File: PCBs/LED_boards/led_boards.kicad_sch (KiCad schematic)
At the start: 14 parts, among them J1 from_shield, J2 from_shield

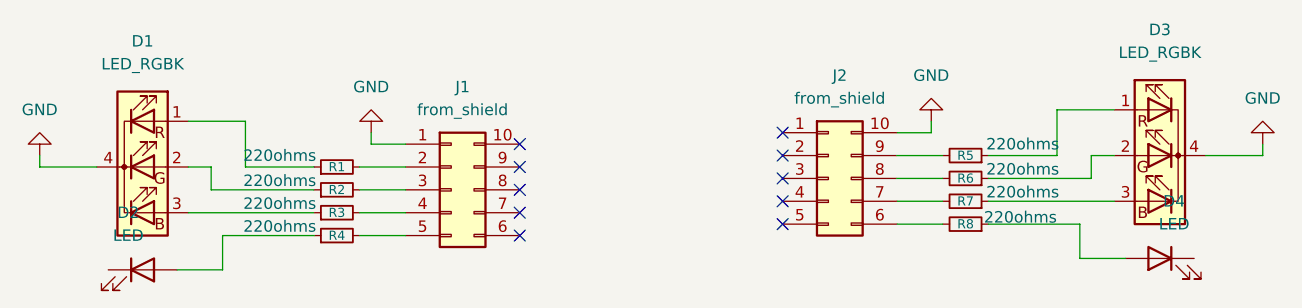
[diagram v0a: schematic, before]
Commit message: create parts for 3D printing
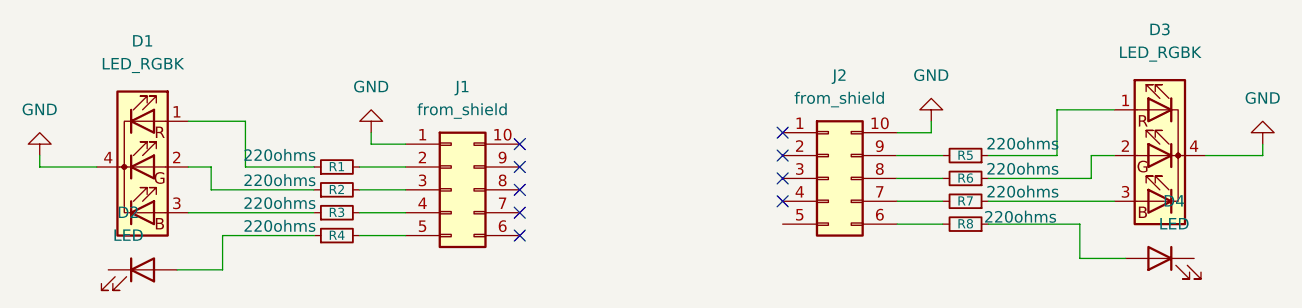
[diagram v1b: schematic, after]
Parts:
- D1, D3: footprint LED_THT:LED_D5.0mm-4_RGB_Wide_Pins -> (none)
- D2, D4: footprint LED_THT:LED_D5.0mm -> (none)
- J1, J2: footprint Connector_IDC:IDC-Header_2x05_P2.54mm_Vertical -> (none)
- R1, R2, R3, R4, R5, R6, R7, R8: footprint Resistor_THT:R_Axial_DIN0309_L9.0mm_D3.2mm_P12.70mm_Horizontal -> (none)
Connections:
- no-connect marks 10 -> 9
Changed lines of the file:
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@@
-	)
-	(no_connect
-		(at 153.67 71.12)
 	)
 	(no_connect
@@
 			)
 		)
-		(property "Footprint" "Resistor_THT:R_Axial_DIN0309_L9.0mm_D3.2mm_P12.70mm_Horizontal"
+		(property "Footprint" ""
 			(at 173.99 63.5 0)
 			(effects
@@
 			)
 		)
-		(property "Footprint" "LED_THT:LED_D5.0mm-4_RGB_Wide_Pins"
+		(property "Footprint" ""
 			(at 195.58 64.77 0)
 			(effects
@@
 			)
 		)
-		(property "Footprint" "Resistor_THT:R_Axial_DIN0309_L9.0mm_D3.2mm_P12.70mm_Horizontal"
+		(property "Footprint" ""
 			(at 104.14 67.31 0)
 			(effects
@@
 			)
 		)
-		(property "Footprint" "Resistor_THT:R_Axial_DIN0309_L9.0mm_D3.2mm_P12.70mm_Horizontal"
+		(property "Footprint" ""
 			(at 173.99 66.04 0)
 			(effects
@@
 			)
 		)
-		(property "Footprint" "Connector_IDC:IDC-Header_2x05_P2.54mm_Vertical"
+		(property "Footprint" ""
 			(at 116.84 67.31 0)
 			(effects
@@
 			)
 		)
-		(property "Footprint" "Resistor_THT:R_Axial_DIN0309_L9.0mm_D3.2mm_P12.70mm_Horizontal"
+		(property "Footprint" ""
 			(at 173.99 68.58 0)
 			(effects
@@
 			)
 		)
-		(property "Footprint" "Connector_IDC:IDC-Header_2x05_P2.54mm_Vertical"
+		(property "Footprint" ""
 			(at 158.75 66.04 0)
 			(effects
@@
 			)
 		)
-		(property "Footprint" "Resistor_THT:R_Axial_DIN0309_L9.0mm_D3.2mm_P12.70mm_Horizontal"
+		(property "Footprint" ""
 			(at 104.14 72.39 0)
 			(effects
@@
 			)
 		)
-		(property "Footprint" "LED_THT:LED_D5.0mm-4_RGB_Wide_Pins"
+		(property "Footprint" ""
 			(at 82.55 66.04 0)
 			(effects
@@
 			)
 		)
-		(property "Footprint" "Resistor_THT:R_Axial_DIN0309_L9.0mm_D3.2mm_P12.70mm_Horizontal"
+		(property "Footprint" ""
 			(at 104.14 69.85 0)
 			(effects
@@
 			)
 		)
-		(property "Footprint" "Resistor_THT:R_Axial_DIN0309_L9.0mm_D3.2mm_P12.70mm_Horizontal"
+		(property "Footprint" ""
 			(at 173.99 71.12 0)
 			(effects
@@
 			)
 		)
-		(property "Footprint" "Resistor_THT:R_Axial_DIN0309_L9.0mm_D3.2mm_P12.70mm_Horizontal"
+		(property "Footprint" ""
 			(at 104.14 64.77 0)
 			(effects
@@
 			)
 		)
-		(property "Footprint" "LED_THT:LED_D5.0mm"
+		(property "Footprint" ""
 			(at 82.55 76.2 0)
 			(effects
@@
 			)
 		)
-		(property "Footprint" "LED_THT:LED_D5.0mm"
+		(property "Footprint" ""
 			(at 195.58 74.93 0)
 			(effects

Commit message: update bom and finish first version of PCBs
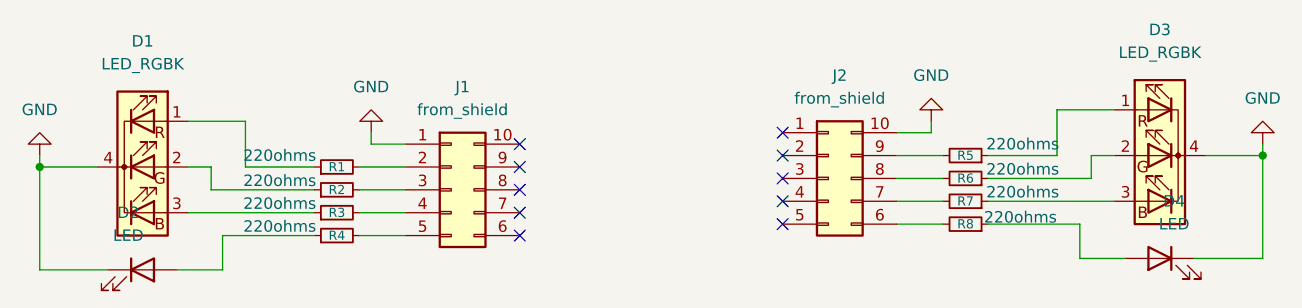
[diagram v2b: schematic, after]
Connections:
- net GND: now also D2.1 (K), D4.1 (K)
- no-connect marks 9 -> 10
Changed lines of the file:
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@@
 	(generator_version "9.0")
 	(paper "A4")
+	(junction
+		(at 207.01 63.5)
+		(diameter 0)
+		(color 0 0 0 0)
+	)
+	(junction
+		(at 71.12 64.77)
+		(diameter 0)
+		(color 0 0 0 0)
+	)
 	(no_connect
 		(at 124.46 72.39)
@@
 		(at 124.46 64.77)
 	)
+	(no_connect
+		(at 153.67 71.12)
+	)
 	(wire
 		(pts
@@
 	(wire
 		(pts
+			(xy 199.39 74.93) (xy 207.01 74.93)
+		)
+		(stroke
+			(width 0)
+			(type default)
+		)
+	)
+	(wire
+		(pts
 			(xy 71.12 64.77) (xy 71.12 63.5)
 		)
@@
 	(wire
 		(pts
+			(xy 207.01 74.93) (xy 207.01 63.5)
+		)
+		(stroke
+			(width 0)
+			(type default)
+		)
+	)
+	(wire
+		(pts
+			(xy 71.12 76.2) (xy 71.12 64.77)
+		)
+		(stroke
+			(width 0)
+			(type default)
+		)
+	)
+	(wire
+		(pts
 			(xy 166.37 68.58) (xy 171.45 68.58)
 		)
@@
 		)
 		(stroke
+			(width 0)
+			(type default)
+		)
+	)
+	(wire
+		(pts
+			(xy 78.74 76.2) (xy 71.12 76.2)
+		)
+		(stroke
